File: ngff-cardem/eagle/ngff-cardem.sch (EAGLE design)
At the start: 147 parts, among them IC201 CB3Q3244PW, IC202 CB3Q3244PW, IC203 IP4234CZ6, IC204 FPF2109, IC205 FPF2109, IC301 TPS22958N-DGN, IC302 TPS22958N-DGK, J301 PJ-002BH-SMT-TR, M2 MENTOR_12701001, M3 MENTOR_12701001, Q201 12MHz, T101 BC850, T102 BC850, U201 IP4234CZ6, U202 AT91SAM3S-AU, U301 MIC5366-1.8YC5, X101 PINHD-2X3-SP, X102 ZX360D-B-10P(30), X201 MINI-USB-SHIELD-UX60-MB-5ST, X202 2.54mm, X203 JACK2.5_SJ-2523, X301 171826-4-RA

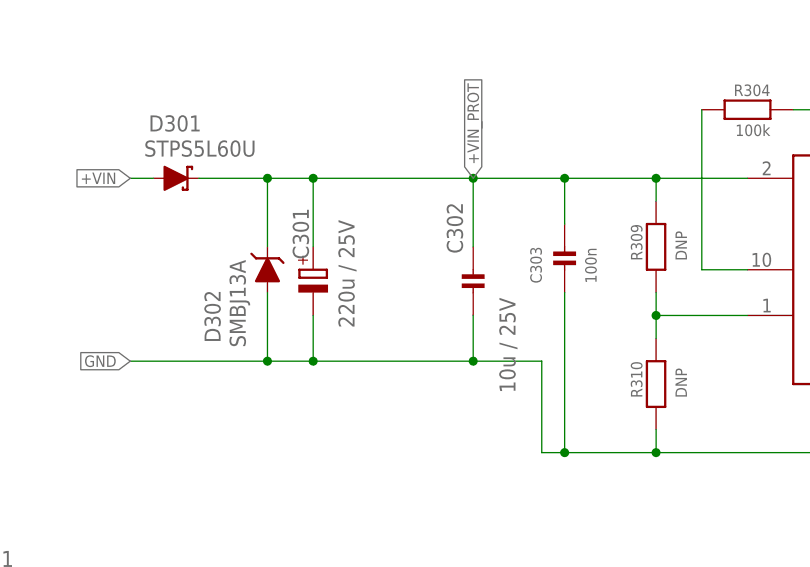
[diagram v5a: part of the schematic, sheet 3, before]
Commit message: ngff-cardem: split C301 into two footprints (solves SYS#5614)
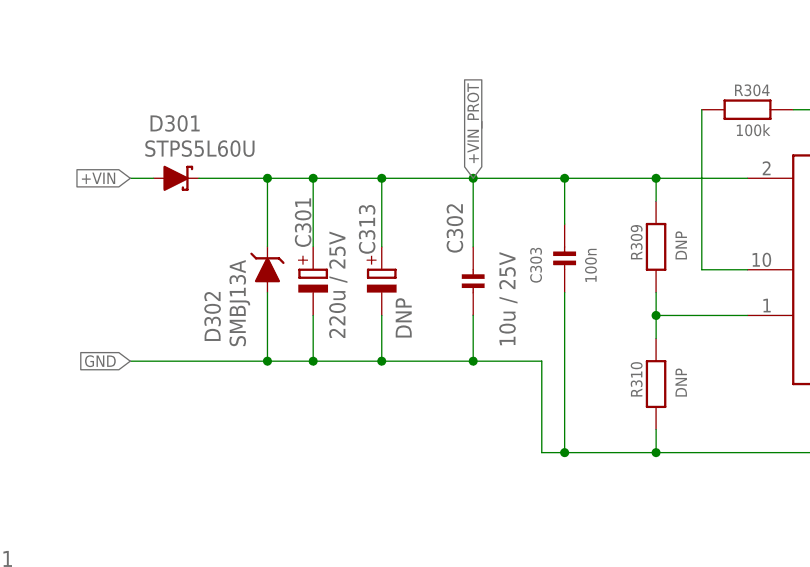
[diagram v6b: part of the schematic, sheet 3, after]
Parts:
- added C313: DNP, rcl:CPOL-EUUD-8X10
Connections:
- net +VIN_PROT: now also C313.+
- net GND: now also C313.-
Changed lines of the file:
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@@
 <attribute name="SOURCEPARTNUMBER" value="UNKNOWN SOURCE PART NUMBER"/>
 </part>
+<part name="C313" library="rcl" deviceset="CPOL-EU" device="UD-8X10" value="DNP">
+<attribute name="CLASS" value="CAPACITOR"/>
+<attribute name="DESCRIPTION" value="NO DESCRIPTION"/>
+<attribute name="LINK" value="UNKNOWN LINK"/>
+<attribute name="MANUFACTURER" value="UNKNOWN MANUFACTURER"/>
+<attribute name="MANUFACTURERPARTNUMBER" value="UNKNOWN MANUFACTURER PART NUMBER"/>
+<attribute name="POPULATED" value="TRUE"/>
+<attribute name="ROHSCERTIFICATE" value="UNKNOWN ROHS CERTIFICATE"/>
+<attribute name="SOURCE" value="UNKNOWN SOURCE"/>
+<attribute name="SOURCEPARTNUMBER" value="UNKNOWN SOURCE PART NUMBER"/>
+</part>
 </parts>
 <sheets>
@@
 <instances>
 <instance part="C301" gate="G$1" x="215.9" y="238.76" smashed="yes">
-<attribute name="NAME" x="215.4174" y="239.903" size="1.778" layer="95" rot="R90"/>
-<attribute name="VALUE" x="220.4974" y="232.283" size="1.778" layer="96" rot="R90"/>
+<attribute name="NAME" x="215.6714" y="241.173" size="1.778" layer="95" rot="R90"/>
+<attribute name="VALUE" x="219.4814" y="231.013" size="1.778" layer="96" rot="R90"/>
 <attribute name="DESCRIPTION" x="215.9" y="238.76" size="1.27" layer="96" display="off"/>
 <attribute name="MANUFACTURER" x="215.9" y="238.76" size="1.27" layer="96" display="off"/>
@@
 <instance part="C302" gate="G$1" x="233.68" y="238.76" smashed="yes" rot="R270">
 <attribute name="NAME" x="232.537" y="240.538" size="1.778" layer="95" rot="R90"/>
-<attribute name="VALUE" x="238.379" y="225.044" size="1.778" layer="96" rot="R90"/>
+<attribute name="VALUE" x="238.379" y="230.124" size="1.778" layer="96" rot="R90"/>
 <attribute name="DESCRIPTION" x="233.68" y="238.76" size="1.778" layer="96" rot="R90" display="off"/>
 <attribute name="MANUFACTURER" x="233.68" y="238.76" size="1.778" layer="96" rot="R90" display="off"/>
@@
 <attribute name="LINK" x="254" y="226.06" size="1.778" layer="96" rot="R270" display="off"/>
 </instance>
+<instance part="C313" gate="G$1" x="223.52" y="238.76" smashed="yes">
+<attribute name="NAME" x="222.7834" y="240.411" size="1.778" layer="95" rot="R90"/>
+<attribute name="VALUE" x="226.8474" y="231.013" size="1.778" layer="96" rot="R90"/>
+<attribute name="DESCRIPTION" x="223.52" y="238.76" size="1.778" layer="96" rot="R90" display="off"/>
+<attribute name="MANUFACTURER" x="223.52" y="238.76" size="1.778" layer="96" rot="R90" display="off"/>
+<attribute name="MANUFACTURERPARTNUMBER" x="223.52" y="238.76" size="1.778" layer="96" rot="R90" display="off"/>
+<attribute name="SOURCE" x="223.52" y="238.76" size="1.778" layer="96" rot="R90" display="off"/>
+<attribute name="SOURCEPARTNUMBER" x="223.52" y="238.76" size="1.778" layer="96" rot="R90" display="off"/>
+<attribute name="ROHSCERTIFICATE" x="223.52" y="238.76" size="1.778" layer="96" rot="R90" display="off"/>
+<attribute name="POPULATED" x="223.52" y="238.76" size="1.778" layer="96" rot="R90" display="off"/>
+<attribute name="CLASS" x="223.52" y="238.76" size="1.778" layer="96" rot="R90" display="off"/>
+<attribute name="LINK" x="223.52" y="238.76" size="1.778" layer="96" rot="R90" display="off"/>
+</instance>
 </instances>
 <busses>
@@
 <wire x1="281.94" y1="215.9" x2="281.94" y2="218.44" width="0.1524" layer="91"/>
 <pinref part="C301" gate="G$1" pin="-"/>
-<wire x1="233.68" y1="228.6" x2="215.9" y2="228.6" width="0.1524" layer="91"/>
+<wire x1="233.68" y1="228.6" x2="223.52" y2="228.6" width="0.1524" layer="91"/>
+<wire x1="223.52" y1="228.6" x2="215.9" y2="228.6" width="0.1524" layer="91"/>
 <wire x1="215.9" y1="228.6" x2="210.82" y2="228.6" width="0.1524" layer="91"/>
 <wire x1="210.82" y1="228.6" x2="195.58" y2="228.6" width="0.1524" layer="91"/>
@@
 <wire x1="254" y1="220.98" x2="254" y2="218.44" width="0.1524" layer="91"/>
 <junction x="254" y="218.44"/>
+<pinref part="C313" gate="G$1" pin="-"/>
+<wire x1="223.52" y1="233.68" x2="223.52" y2="228.6" width="0.1524" layer="91"/>
+<junction x="223.52" y="228.6"/>
 </segment>
 <segment>
@@
 <wire x1="233.68" y1="241.3" x2="233.68" y2="248.92" width="0.1524" layer="91"/>
 <pinref part="C301" gate="G$1" pin="+"/>
-<wire x1="233.68" y1="248.92" x2="215.9" y2="248.92" width="0.1524" layer="91"/>
+<wire x1="233.68" y1="248.92" x2="223.52" y2="248.92" width="0.1524" layer="91"/>
+<wire x1="223.52" y1="248.92" x2="215.9" y2="248.92" width="0.1524" layer="91"/>
 <wire x1="215.9" y1="241.3" x2="215.9" y2="248.92" width="0.1524" layer="91"/>
 <junction x="215.9" y="248.92"/>
@@
 <wire x1="254" y1="246.38" x2="254" y2="248.92" width="0.1524" layer="91"/>
 <junction x="254" y="248.92"/>
+<pinref part="C313" gate="G$1" pin="+"/>
+<wire x1="223.52" y1="241.3" x2="223.52" y2="248.92" width="0.1524" layer="91"/>
+<junction x="223.52" y="248.92"/>
 </segment>
 </net>

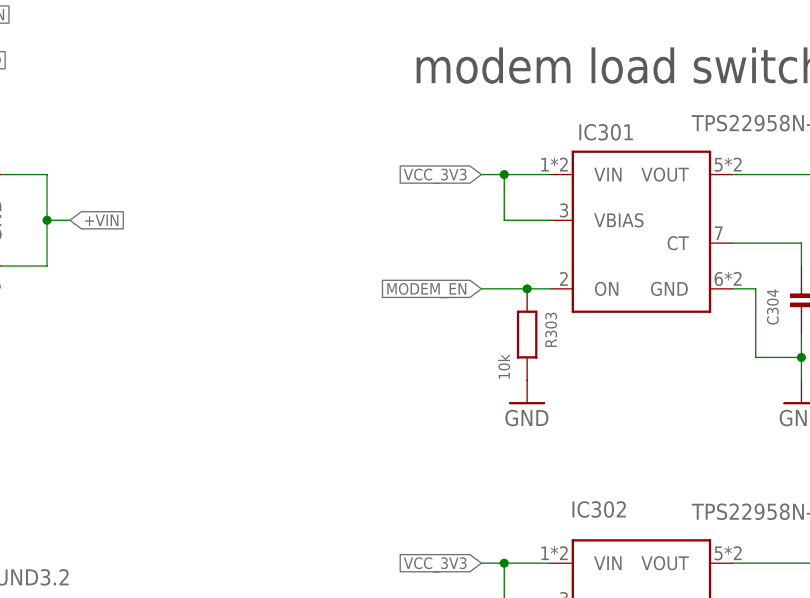
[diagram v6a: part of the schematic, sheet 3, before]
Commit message: ngff-cardem: unconditionally enable PWR switch (solves SYS#5520)
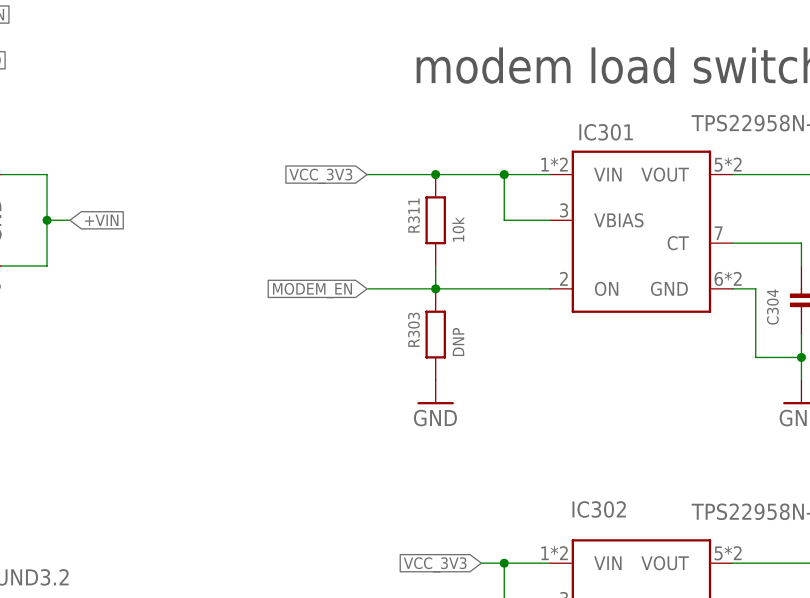
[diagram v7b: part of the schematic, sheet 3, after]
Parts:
- added R311: 10k, rc-sysmocom:RESISTOR_0603
- R303: value 10k -> DNP; DESCRIPTION RES SMD 10K OHM 1%% 1/10W 0603 -> NO DESCRIPTION; LINK https://www.digikey.de/product-detail/de/te-connectivity-pa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 -> UNKNOWN LINK; MANUFACTURER TE Connectivity Passive Product -> UNKNOWN MANUFACTURER; MANUFACTURERPARTNUMBER CRG0603F10K/10 -> UNKNOWN MANUFACTURER PART NUMBER; POPULATED TRUE -> FALSE; ROHSCERTIFICATE RoHS-konform -> UNKNOWN ROHS CERTIFICATE; SOURCE DIGIKEY -> UNKNOWN SOURCE; SOURCEPARTNUMBER A121523CT-ND -> UNKNOWN SOURCE PART NUMBER
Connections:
- net MODEM_EN: now also R311.1
- net VCC_3V3: now also R311.2
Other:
- moved on the sheet: R303
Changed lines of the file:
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@@
 <variant name="LEDs bott" populate="no"/>
 </part>
-<part name="R303" library="rc-sysmocom" deviceset="RESISTOR" device="_0603" value="10k">
+<part name="R303" library="rc-sysmocom" deviceset="RESISTOR" device="_0603" value="DNP">
 <attribute name="CLASS" value="RESISTOR"/>
-<attribute name="DESCRIPTION" value="RES SMD 10K OHM 1%% 1/10W 0603"/>
-<attribute name="LINK" value="https://www.digikey.de/product-detail/de/te-connectivity-passive-product/CRG0603F10K-10/A121523CT-ND/"/>
-<attribute name="MANUFACTURER" value="TE Connectivity Passive Product"/>
-<attribute name="MANUFACTURERPARTNUMBER" value="CRG0603F10K/10"/>
-<attribute name="POPULATED" value="TRUE"/>
-<attribute name="ROHSCERTIFICATE" value="RoHS-konform"/>
-<attribute name="SOURCE" value="DIGIKEY"/>
-<attribute name="SOURCEPARTNUMBER" value="A121523CT-ND"/>
+<attribute name="DESCRIPTION" value="NO DESCRIPTION"/>
+<attribute name="LINK" value="UNKNOWN LINK"/>
+<attribute name="MANUFACTURER" value="UNKNOWN MANUFACTURER"/>
+<attribute name="MANUFACTURERPARTNUMBER" value="UNKNOWN MANUFACTURER PART NUMBER"/>
+<attribute name="POPULATED" value="FALSE"/>
+<attribute name="ROHSCERTIFICATE" value="UNKNOWN ROHS CERTIFICATE"/>
+<attribute name="SOURCE" value="UNKNOWN SOURCE"/>
+<attribute name="SOURCEPARTNUMBER" value="UNKNOWN SOURCE PART NUMBER"/>
 </part>
 <part name="GND6" library="supply1" deviceset="GND" device=""/>
@@
 <attribute name="SOURCEPARTNUMBER" value="UNKNOWN SOURCE PART NUMBER"/>
 </part>
+<part name="R311" library="rc-sysmocom" deviceset="RESISTOR" device="_0603" value="10k">
+<attribute name="CLASS" value="RESISTOR"/>
+<attribute name="DESCRIPTION" value="RES SMD 10K OHM 1%% 1/10W 0603"/>
+<attribute name="LINK" value="https://www.digikey.de/product-detail/de/te-connectivity-passive-product/CRG0603F10K-10/A121523CT-ND/"/>
+<attribute name="MANUFACTURER" value="TE Connectivity Passive Product"/>
+<attribute name="MANUFACTURERPARTNUMBER" value="CRG0603F10K/10"/>
+<attribute name="POPULATED" value="TRUE"/>
+<attribute name="ROHSCERTIFICATE" value="RoHS-konform"/>
+<attribute name="SOURCE" value="DIGIKEY"/>
+<attribute name="SOURCEPARTNUMBER" value="A121523CT-ND"/>
+</part>
 </parts>
 <sheets>
@@
 <attribute name="LINK" x="180.34" y="119.38" size="1.778" layer="96" display="off"/>
 </instance>
-<instance part="R303" gate="G$1" x="259.08" y="167.64" smashed="yes" rot="R90">
-<attribute name="NAME" x="262.382" y="166.116" size="1.27" layer="95" font="vector" rot="R90"/>
-<attribute name="VALUE" x="257.175" y="162.56" size="1.27" layer="96" font="vector" rot="R90"/>
-<attribute name="DESCRIPTION" x="259.08" y="167.64" size="1.778" layer="96" display="off"/>
-<attribute name="MANUFACTURER" x="259.08" y="167.64" size="1.778" layer="96" display="off"/>
-<attribute name="MANUFACTURERPARTNUMBER" x="259.08" y="167.64" size="1.778" layer="96" display="off"/>
-<attribute name="SOURCE" x="259.08" y="167.64" size="1.778" layer="96" display="off"/>
-<attribute name="SOURCEPARTNUMBER" x="259.08" y="167.64" size="1.778" layer="96" display="off"/>
-<attribute name="ROHSCERTIFICATE" x="259.08" y="167.64" size="1.778" layer="96" display="off"/>
-<attribute name="POPULATED" x="259.08" y="167.64" size="1.778" layer="96" display="off"/>
-<attribute name="CLASS" x="259.08" y="167.64" size="1.778" layer="96" display="off"/>
-<attribute name="LINK" x="259.08" y="167.64" size="1.778" layer="96" display="off"/>
+<instance part="R303" gate="G$1" x="248.92" y="167.64" smashed="yes" rot="R90">
+<attribute name="NAME" x="247.142" y="166.116" size="1.27" layer="95" font="vector" rot="R90"/>
+<attribute name="VALUE" x="252.095" y="165.1" size="1.27" layer="96" font="vector" rot="R90"/>
+<attribute name="DESCRIPTION" x="248.92" y="167.64" size="1.778" layer="96" rot="R90" display="off"/>
+<attribute name="MANUFACTURER" x="248.92" y="167.64" size="1.778" layer="96" rot="R90" display="off"/>
+<attribute name="MANUFACTURERPARTNUMBER" x="248.92" y="167.64" size="1.778" layer="96" rot="R90" display="off"/>
+<attribute name="SOURCE" x="248.92" y="167.64" size="1.778" layer="96" rot="R90" display="off"/>
+<attribute name="SOURCEPARTNUMBER" x="248.92" y="167.64" size="1.778" layer="96" rot="R90" display="off"/>
+<attribute name="ROHSCERTIFICATE" x="248.92" y="167.64" size="1.778" layer="96" rot="R90" display="off"/>
+<attribute name="POPULATED" x="248.92" y="167.64" size="1.778" layer="96" rot="R90" display="off"/>
+<attribute name="CLASS" x="248.92" y="167.64" size="1.778" layer="96" rot="R90" display="off"/>
+<attribute name="LINK" x="248.92" y="167.64" size="1.778" layer="96" rot="R90" display="off"/>
 </instance>
-<instance part="GND6" gate="1" x="259.08" y="160.02"/>
+<instance part="GND6" gate="1" x="248.92" y="160.02"/>
 <instance part="R305" gate="G$1" x="335.28" y="226.06" rot="R90">
 <attribute name="DESCRIPTION" x="335.28" y="226.06" size="1.778" layer="96" display="off"/>
@@
 <attribute name="LINK" x="223.52" y="238.76" size="1.778" layer="96" rot="R90" display="off"/>
 </instance>
+<instance part="R311" gate="G$1" x="248.92" y="180.34" smashed="yes" rot="R90">
+<attribute name="NAME" x="247.142" y="178.816" size="1.27" layer="95" font="vector" rot="R90"/>
+<attribute name="VALUE" x="252.095" y="177.8" size="1.27" layer="96" font="vector" rot="R90"/>
+<attribute name="DESCRIPTION" x="248.92" y="180.34" size="1.778" layer="96" display="off"/>
+<attribute name="MANUFACTURER" x="248.92" y="180.34" size="1.778" layer="96" display="off"/>
+<attribute name="MANUFACTURERPARTNUMBER" x="248.92" y="180.34" size="1.778" layer="96" display="off"/>
+<attribute name="SOURCE" x="248.92" y="180.34" size="1.778" layer="96" display="off"/>
+<attribute name="SOURCEPARTNUMBER" x="248.92" y="180.34" size="1.778" layer="96" display="off"/>
+<attribute name="ROHSCERTIFICATE" x="248.92" y="180.34" size="1.778" layer="96" display="off"/>
+<attribute name="POPULATED" x="248.92" y="180.34" size="1.778" layer="96" display="off"/>
+<attribute name="CLASS" x="248.92" y="180.34" size="1.778" layer="96" display="off"/>
+<attribute name="LINK" x="248.92" y="180.34" size="1.778" layer="96" display="off"/>
+</instance>
 </instances>
 <busses>
@@
 <segment>
 <pinref part="IC301" gate="G$1" pin="ON"/>
-<wire x1="261.62" y1="172.72" x2="259.08" y2="172.72" width="0.1524" layer="91"/>
-<label x="254" y="172.72" size="1.27" layer="95" rot="R180" xref="yes"/>
+<wire x1="261.62" y1="172.72" x2="248.92" y2="172.72" width="0.1524" layer="91"/>
+<label x="241.3" y="172.72" size="1.27" layer="95" rot="R180" xref="yes"/>
 <pinref part="R303" gate="G$1" pin="2"/>
-<wire x1="259.08" y1="172.72" x2="254" y2="172.72" width="0.1524" layer="91"/>
-<junction x="259.08" y="172.72"/>
+<wire x1="248.92" y1="172.72" x2="241.3" y2="172.72" width="0.1524" layer="91"/>
+<junction x="248.92" y="172.72"/>
+<pinref part="R311" gate="G$1" pin="1"/>
+<wire x1="248.92" y1="175.26" x2="248.92" y2="172.72" width="0.1524" layer="91"/>
 </segment>
 <segment>
@@
 <pinref part="IC301" gate="G$1" pin="VIN"/>
 <wire x1="256.54" y1="185.42" x2="261.62" y2="185.42" width="0.1524" layer="91"/>
-<wire x1="254" y1="185.42" x2="256.54" y2="185.42" width="0.1524" layer="91"/>
+<wire x1="241.3" y1="185.42" x2="248.92" y2="185.42" width="0.1524" layer="91"/>
 <junction x="256.54" y="185.42"/>
-<label x="254" y="185.42" size="1.27" layer="95" rot="R180" xref="yes"/>
+<label x="241.3" y="185.42" size="1.27" layer="95" rot="R180" xref="yes"/>
+<pinref part="R311" gate="G$1" pin="2"/>
+<wire x1="248.92" y1="185.42" x2="256.54" y2="185.42" width="0.1524" layer="91"/>
+<junction x="248.92" y="185.42"/>
 </segment>
 <segment>

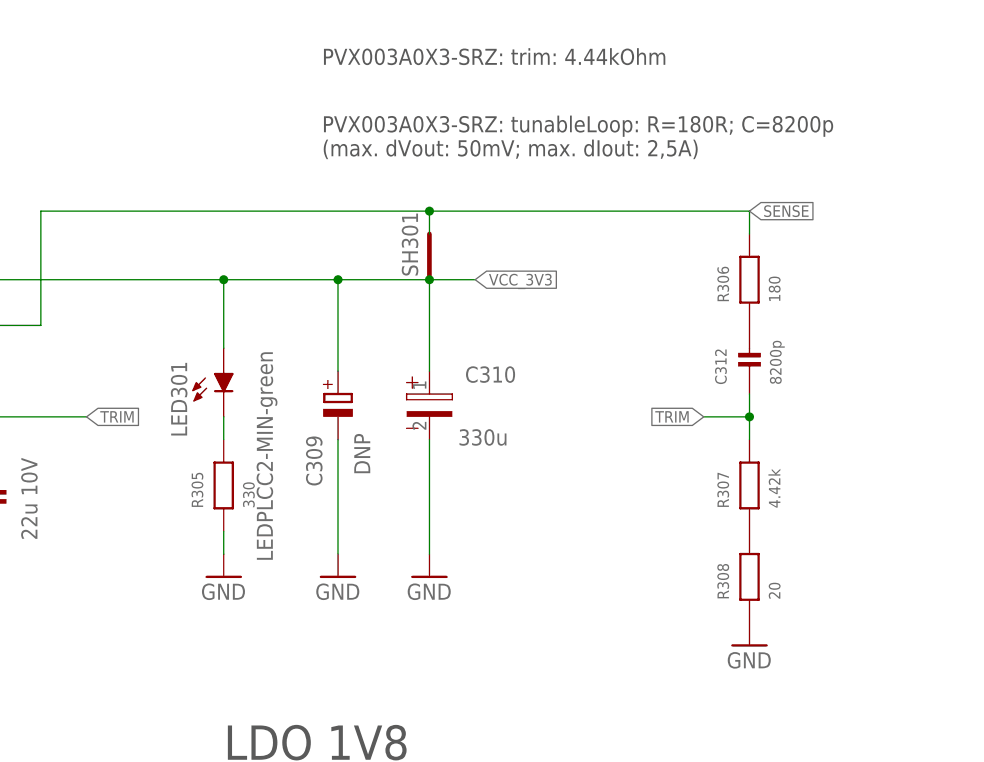
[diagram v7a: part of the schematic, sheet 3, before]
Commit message: ngff-cardem: adjust setting resistors for Murata OKL (solves SYS#5613)
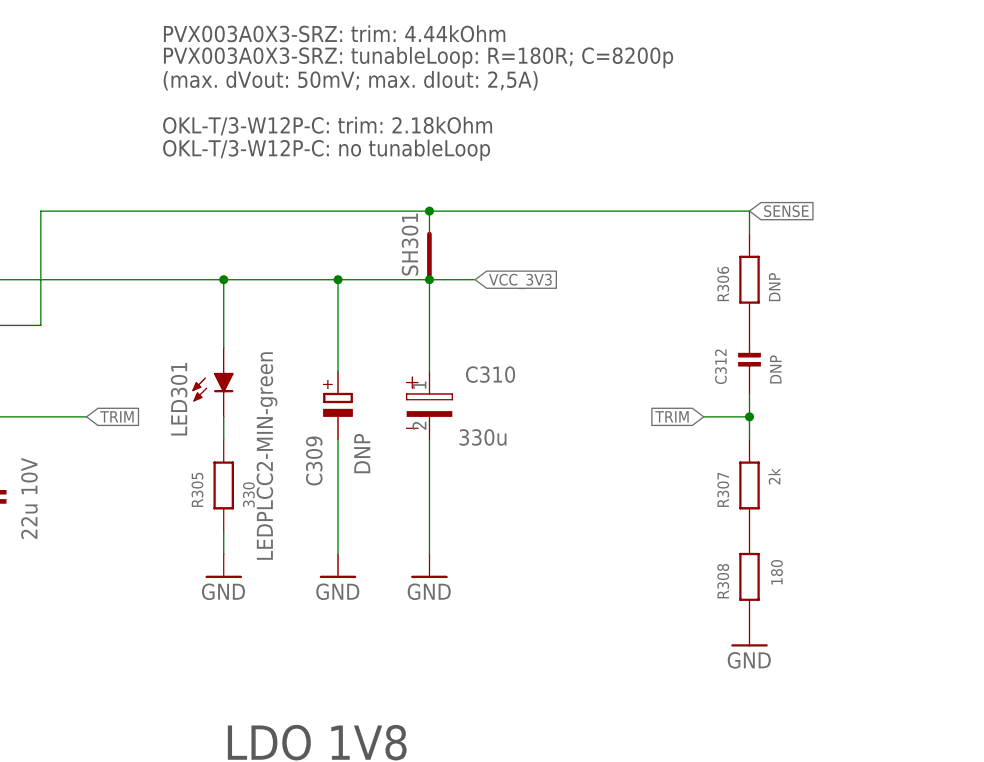
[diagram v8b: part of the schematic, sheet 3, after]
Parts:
- C312: value 8200p -> DNP; DESCRIPTION CAP CER 8200PF 50V C0G/NP0 0603 -> NO DESCRIPTION; LINK https://www.digikey.de/product-detail/de/murata-electronics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 -> UNKNOWN LINK; MANUFACTURER Murata Electronics -> UNKNOWN MANUFACTURER; MANUFACTURERPARTNUMBER GRM1885C1H822JA01D -> UNKNOWN MANUFACTURER PART NUMBER; POPULATED TRUE -> FALSE; ROHSCERTIFICATE RoHS3-konform -> UNKNOWN ROHS CERTIFICATE; SOURCE DIGIKEY -> UNKNOWN SOURCE; SOURCEPARTNUMBER 490-11482-1-ND -> UNKNOWN SOURCE PART NUMBER
- R306: value 180 -> DNP; DESCRIPTION RES SMD 180 OHM 1%% 1/10W 0603 -> NO DESCRIPTION; LINK https://www.digikey.de/product-detail/de/yageo/RC0603FR-071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 -> UNKNOWN LINK; MANUFACTURER Yageo -> UNKNOWN MANUFACTURER; MANUFACTURERPARTNUMBER RC0603FR-07180RL -> UNKNOWN MANUFACTURER PART NUMBER; POPULATED TRUE -> FALSE; ROHSCERTIFICATE RoHS3-konform -> UNKNOWN ROHS CERTIFICATE; SOURCE DIGIKEY -> UNKNOWN SOURCE; SOURCEPARTNUMBER 311-180HRCT-ND -> UNKNOWN SOURCE PART NUMBER
- R307: value 4.42k -> 2k; DESCRIPTION RES SMD 4.42KOHM 0.1%% 1/10W 0603 -> RES SMD 2K OHM 1% 1/10W 0603; LINK https://www.digikey.de/product-detail/de/panasonic-electron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 -> https://www.digikey.de/product-detail/de/yageo/RC0603FR-072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; MANUFACTURER Panasonic Electronic Components -> YAGEO; MANUFACTURERPARTNUMBER ERA-3AEB4421V -> RC0603FR-072KL; SOURCEPARTNUMBER P4.42KDBCT-ND -> 311-2.00KHRCT-ND
- R308: value 20 -> 180; DESCRIPTION RES SMD 20 OHM 1%% 1/10W 0603 -> RES SMD 180R 1% 1/10W 0603; LINK https://www.digikey.de/product-detail/de/yageo/RC0603FR-072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 -> https://www.digikey.de/product-detail/de/te-connectivity-pa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; MANUFACTURER Yageo -> TE Connectivity Passive Product; MANUFACTURERPARTNUMBER RC0603FR-0720RL -> CRGCQ0603F180R; SOURCEPARTNUMBER 311-20.0HRCT-ND -> A129679CT-ND
- X201: DESCRIPTION NO DESCRIPTION -> (none); MANUFACTURER UNKNOWN MANUFACTURER -> (none); MANUFACTURERPARTNUMBER UNKNOWN MANUFACTURER PART NUMBER -> (none); ROHSCERTIFICATE UNKNOWN ROHS CERTIFICATE -> (none); SOURCEPARTNUMBER UNKNOWN SOURCE PART NUMBER -> (none)
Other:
- note added: "OKL-T/3-W12P-C: no tunableLoop"
- note added: "OKL-T/3-W12P-C: trim: 2.18kOhm"
